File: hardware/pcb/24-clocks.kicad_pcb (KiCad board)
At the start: 2 copper layers, 94 x 84 mm, 89 parts, among them J201 ST-LINK, J202 Debug UART, J401 S4B_XH_SM4_TB, J402 S4B_XH_SM4_TB, J601 Conn_02x03_Odd_Even, U201 STM32F103C8Tx, U301 VID28-05, U302 VID66-08, U303 AH3572, U304 AH3572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

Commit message: changed outputs
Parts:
- moved H104 0.54 mm to (128.0, 135.0)
- moved H102 0.32 mm to (172.0, 135.0)

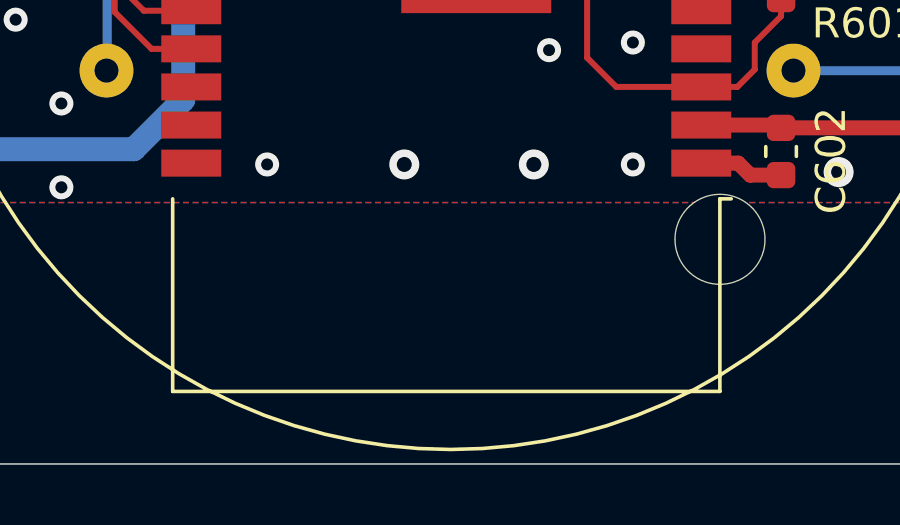
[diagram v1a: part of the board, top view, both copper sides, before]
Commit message: Added layer to output
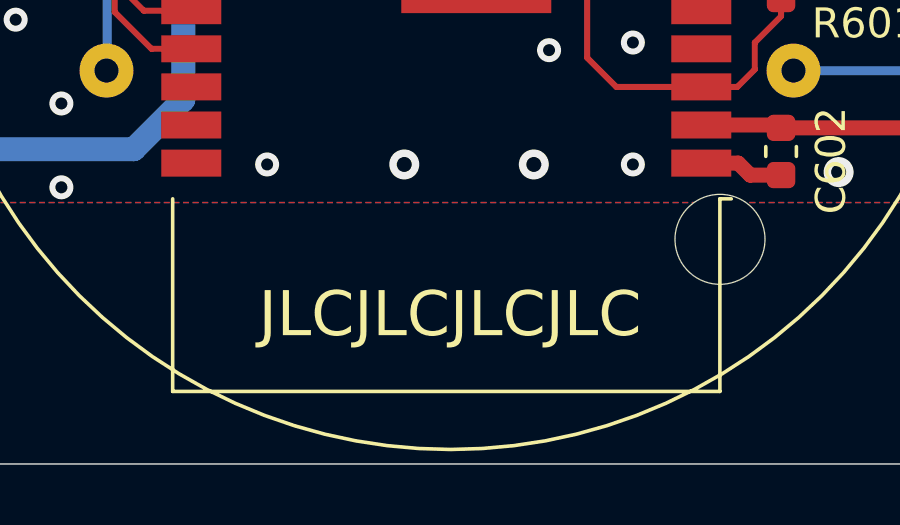
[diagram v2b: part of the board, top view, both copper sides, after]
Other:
- board text added: "JLCJLCJLCJLC"

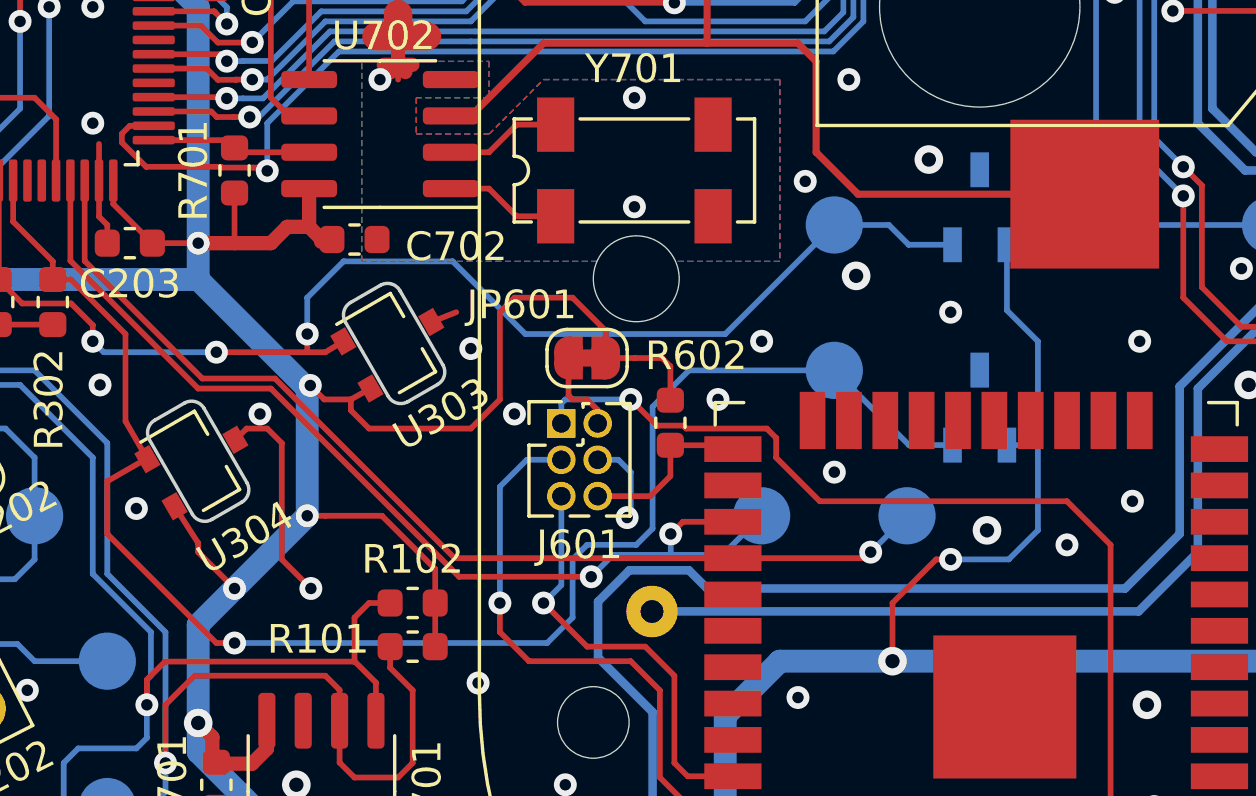
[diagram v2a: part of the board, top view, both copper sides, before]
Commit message: Added caps to hall sensors
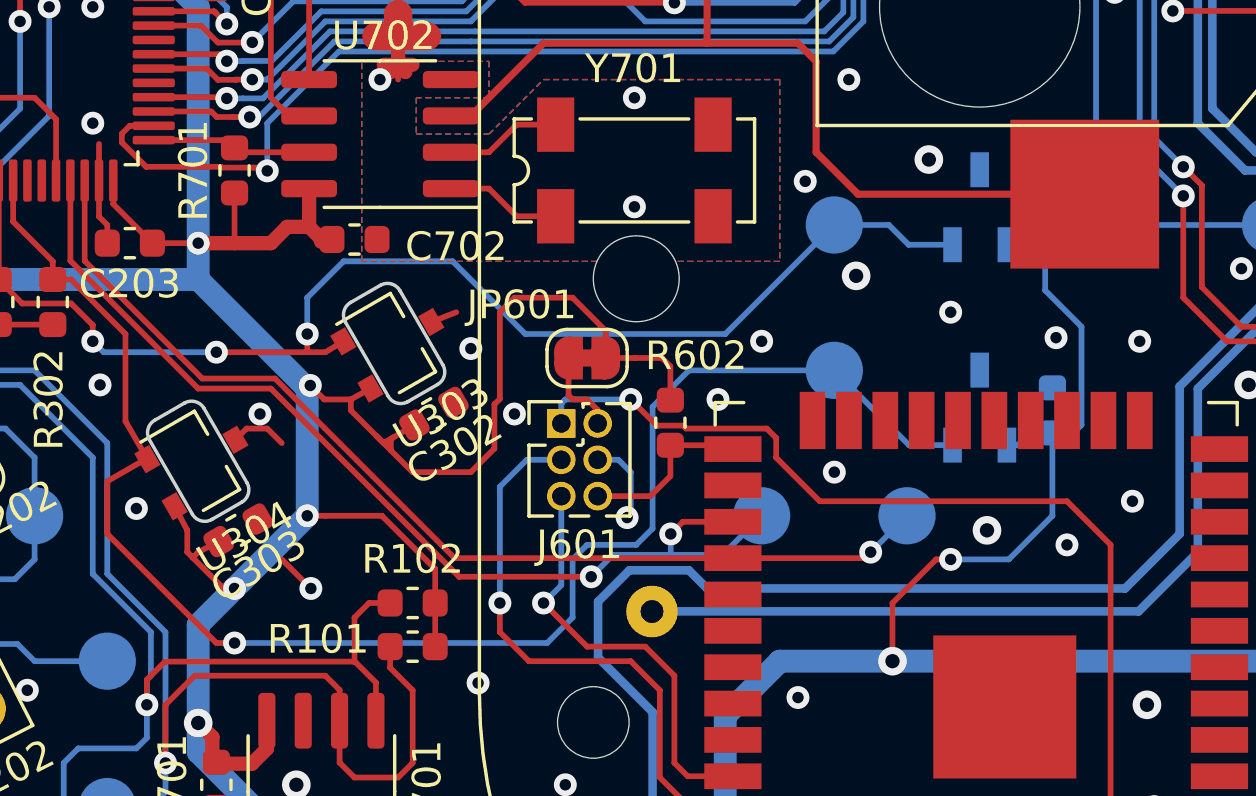
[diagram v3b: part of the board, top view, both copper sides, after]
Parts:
- added C302: 100nF, Capacitor_SMD:C_0603_1608Metric, F.Cu at (130.9, 114.2)
- added C303: 100nF, Capacitor_SMD:C_0603_1608Metric, F.Cu at (124.1, 118.3)
- added C304: 100nF, Capacitor_SMD:C_0603_1608Metric, B.Cu at (152.3, 107.0)
- added C305: 100nF, Capacitor_SMD:C_0603_1608Metric, B.Cu at (152.5, 114.1)
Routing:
- net +3V3: track 313.7 -> 323.4 mm
- net GND: track 86.2 -> 82.1 mm, vias 133 -> 134
